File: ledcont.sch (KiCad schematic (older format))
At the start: 22 parts, among them J1 Screw_Terminal_01x02, J2 Screw_Terminal_01x02, U1 PAM2804, U2 TSM102A

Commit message: Switched PAM2804 to a standard TSOT-23-5 footprint.
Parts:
- U1: footprint ledcont:TSOT25 -> Package_TO_SOT_SMD:TSOT-23-5_HandSoldering
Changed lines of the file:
@@
 F 0 "U1" H 6550 2665 50  0000 C CNN
 F 1 "PAM2804" H 6550 2574 50  0000 C CNN
-F 2 "ledcont:TSOT25" H 6550 2250 50  0001 C CNN
+F 2 "Package_TO_SOT_SMD:TSOT-23-5_HandSoldering" H 6550 2250 50  0001 C CNN
 F 3 "" H 6550 2250 50  0001 C CNN
 F 4 "PAM2804AAB010" H 0   0   50  0001 C CNN "Part"

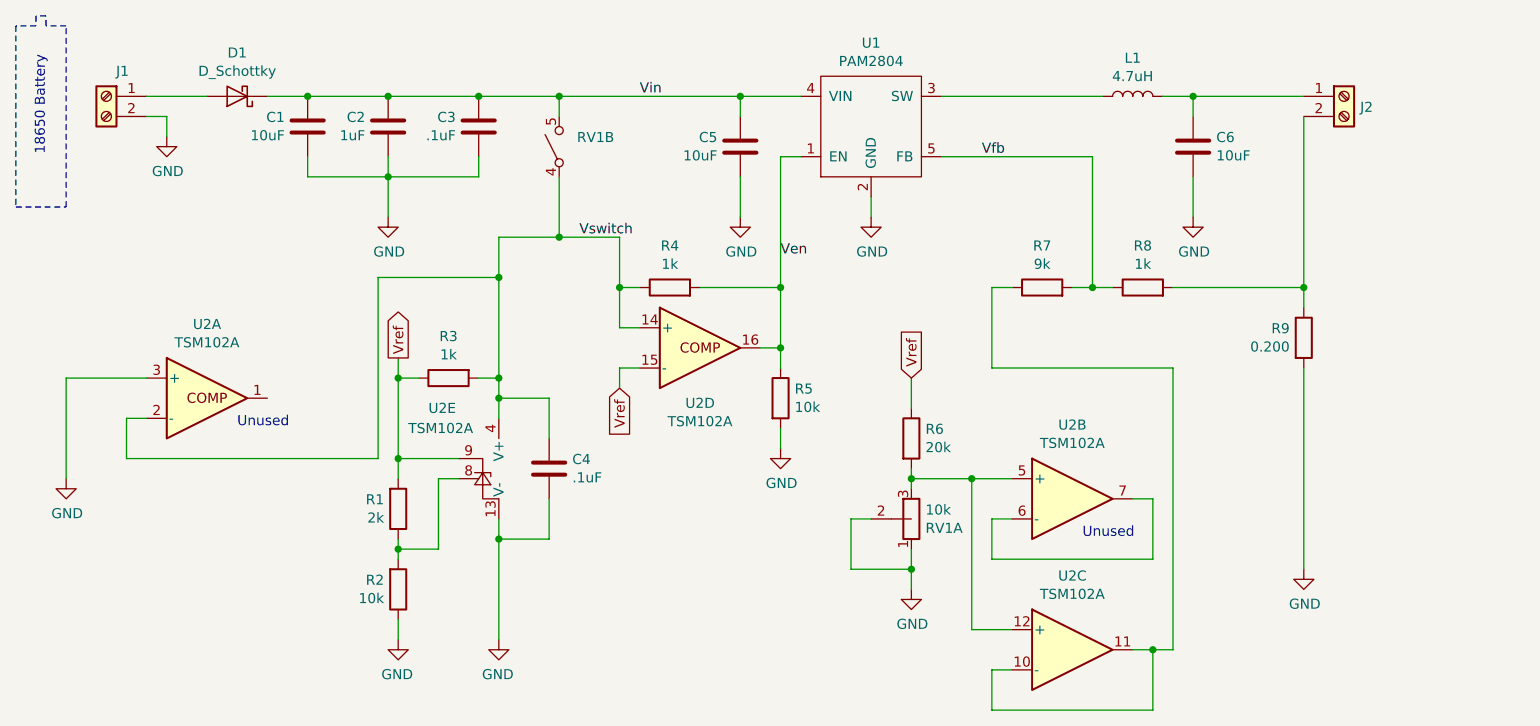
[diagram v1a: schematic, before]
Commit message: Start transitioning to lower-voltage parts.
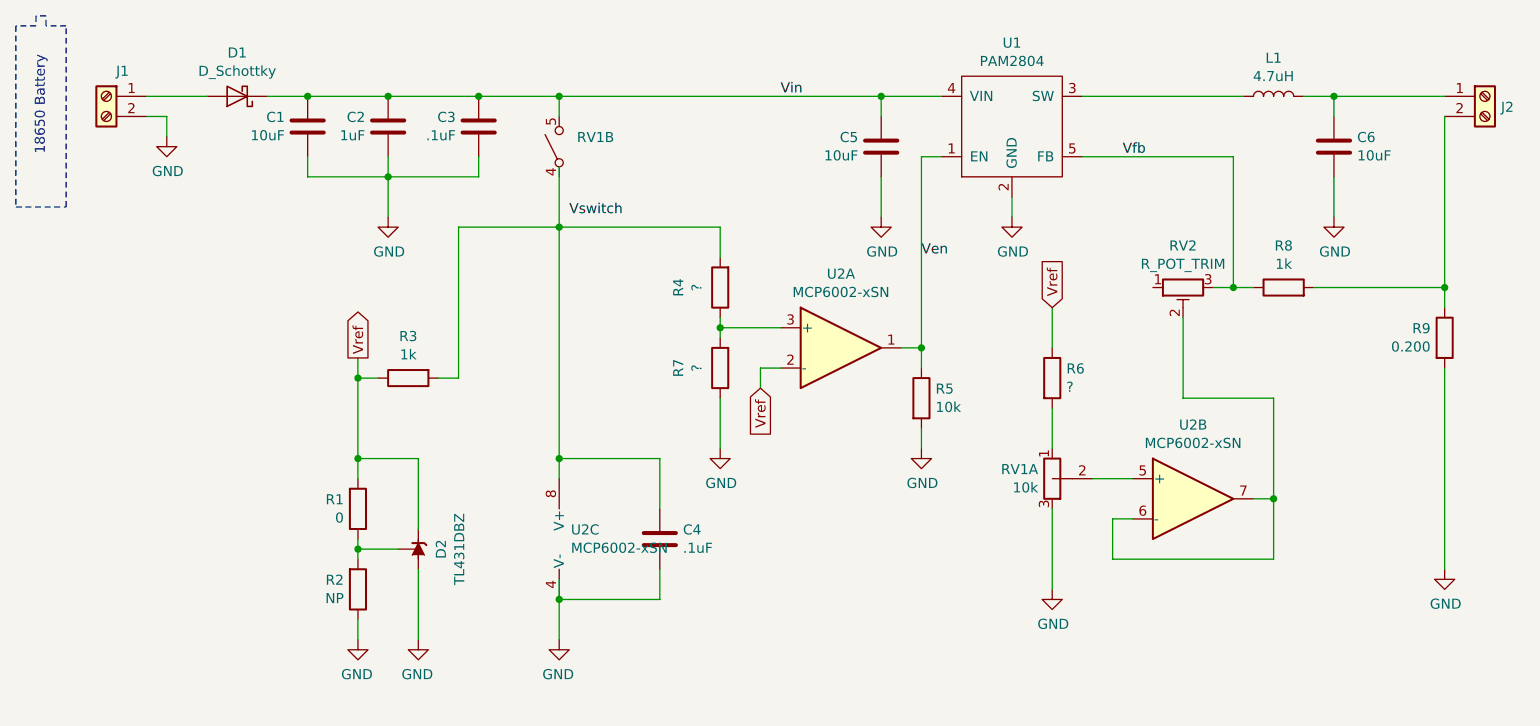
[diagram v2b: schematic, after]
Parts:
- removed U2: TSM102A, Package_SO:SOIC-16_3.9x9.9mm_P1.27mm, symbol Power_Management:TSM102A
- added D2: TL431DBZ, Package_TO_SOT_SMD:SOT-23, symbol Reference_Voltage:TL431DBZ
- added RV2: R_POT_TRIM, symbol Device:R_POT_TRIM
- added U2: MCP6002-xSN, Package_SO:SOIC-8_3.9x4.9mm_P1.27mm, symbol Amplifier_Operational:MCP6002-xSN
- R1: value 2k -> 0
- R2: value 10k -> NP
- R4: value 1k -> ?
- R6: value 20k -> ?
- R7: value 9k -> ?
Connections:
- net GND: now also R7.1, RV1.3, D2.3 (A), U2.4 (V-); no longer RV1.1, RV1.2 (B)
- net Ven: now also U2.1; no longer R4.2
- net Vfb: now also RV2.3; no longer R7.2
- net Vref: now also D2.1 (K), U2.2 (-)
- net Vswitch: no longer C4.1, R3.2, R4.1, RV1.4
- net at R6.2: now also RV1.1; no longer RV1.3
- net at R1.1, R2.2: now also D2.2 (REF)
- new net: RV1.2 (B), U2.5 (+)
- new net: C4.1, R3.2, R4.2, U2.8 (V+)
- new net: R4.1, R7.2, U2.3 (+)
- new net: RV2.2, U2.6 (-), U2.7
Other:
- note removed: "Unused"
- moved on the sheet: C4, C5, C6, J2, L1, R1, R2, R3, R5, R6, R8, R9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

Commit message: More board updates.
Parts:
- added R10: 10k, Resistor_SMD:R_0603_1608Metric_Pad1.05x0.95mm_HandSolder, symbol Device:R
- added R11, R12: 0, Resistor_SMD:R_0603_1608Metric_Pad1.05x0.95mm_HandSolder, symbol Device:R
- D2: value TL431DBZ -> TLV431
- R1, R2, R3, R5: footprint Resistor_SMD:R_1206_3216Metric_Pad1.42x1.75mm_HandSolder -> Resistor_SMD:R_0603_1608Metric_Pad1.05x0.95mm_HandSolder
- R4: value ? -> 10k; footprint Resistor_SMD:R_1206_3216Metric_Pad1.42x1.75mm_HandSolder -> Resistor_SMD:R_0603_1608Metric_Pad1.05x0.95mm_HandSolder
- R6: value ? -> 0; footprint Resistor_SMD:R_1206_3216Metric_Pad1.42x1.75mm_HandSolder -> Resistor_SMD:R_0603_1608Metric_Pad1.05x0.95mm_HandSolder
- R7: value ? -> 7k; footprint Resistor_SMD:R_1206_3216Metric_Pad1.42x1.75mm_HandSolder -> Resistor_SMD:R_0603_1608Metric_Pad1.05x0.95mm_HandSolder
- RV2: value R_POT_TRIM -> 5k; footprint (none) -> ledcont:TC33X
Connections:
- net Ven: now also R12.2; no longer U1.1 (EN)
- net Vfb: now also R10.2; no longer RV2.3
- net Vswitch: now also C4.1, R3.2, R4.2, RV1.4, U2.8 (V+)
- net at U2.6 (-), U2.7: now also R11.2; no longer RV2.2
- net at RV2.1: now also RV2.2, R11.1
- new net: R12.1, U1.1 (EN)
- new net: R10.1, RV2.3
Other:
- moved on the sheet: R6, RV1A, RV2
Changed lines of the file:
@@
 L ledcont:R_POT_SPST RV1
 U 1 1 5C458CC6
-P 7450 4000
-F 0 "RV1" H 7380 3954 50  0000 R CNN
-F 1 "10k" H 7380 4045 50  0000 R CNN
-F 2 "ledcont:P091_S" H 7450 4000 50  0001 C CNN
-F 3 "~" H 7450 4000 50  0001 C CNN
-F 4 "P091S-FC20BR10K" H 700 -200 50  0001 C CNN "Part"
-	1    7450 4000
+P 7250 4000
+F 0 "RV1" H 7180 3954 50  0000 R CNN
+F 1 "10k" H 7180 4045 50  0000 R CNN
+F 2 "ledcont:P091_S" H 7250 4000 50  0001 C CNN
+F 3 "~" H 7250 4000 50  0001 C CNN
+F 4 "P091S-FC20BR10K" H 500 -200 50  0001 C CNN "Part"
+	1    7250 4000
 	1    0    0    1
 $EndComp
@@
 F 0 "R3" V 4043 3500 50  0000 C CNN
 F 1 "1k" V 4134 3500 50  0000 C CNN
-F 2 "Resistor_SMD:R_1206_3216Metric_Pad1.42x1.75mm_HandSolder" V 4180 3500 50  0001 C CNN
+F 2 "Resistor_SMD:R_0603_1608Metric_Pad1.05x0.95mm_HandSolder" V 4180 3500 50  0001 C CNN
 F 3 "~" H 4250 3500 50  0001 C CNN
 F 4 "1%" H -200 0   50  0001 C CNN "Tolerance"
@@
 F 0 "R1" H 3930 4104 50  0000 R CNN
 F 1 "0" H 3930 4195 50  0000 R CNN
-F 2 "Resistor_SMD:R_1206_3216Metric_Pad1.42x1.75mm_HandSolder" V 3930 4150 50  0001 C CNN
+F 2 "Resistor_SMD:R_0603_1608Metric_Pad1.05x0.95mm_HandSolder" V 3930 4150 50  0001 C CNN
 F 3 "~" H 4000 4150 50  0001 C CNN
 F 4 "1%" H 4000 4150 50  0001 C CNN "Tolerance"
@@
 F 0 "R2" H 3930 4504 50  0000 R CNN
 F 1 "NP" H 3930 4595 50  0000 R CNN
-F 2 "Resistor_SMD:R_1206_3216Metric_Pad1.42x1.75mm_HandSolder" V 3930 4550 50  0001 C CNN
+F 2 "Resistor_SMD:R_0603_1608Metric_Pad1.05x0.95mm_HandSolder" V 3930 4550 50  0001 C CNN
 F 3 "~" H 4000 4550 50  0001 C CNN
 F 4 "1%" H -200 0   50  0001 C CNN "Tolerance"
@@
 L Device:R R6
 U 1 1 5C482FDC
-P 7450 3500
-F 0 "R6" H 7520 3546 50  0000 L CNN
-F 1 "?" H 7520 3455 50  0000 L CNN
-F 2 "Resistor_SMD:R_1206_3216Metric_Pad1.42x1.75mm_HandSolder" V 7380 3500 50  0001 C CNN
-F 3 "~" H 7450 3500 50  0001 C CNN
-F 4 "RC1206FR-0720KL" H 700 -300 50  0001 C CNN "Part"
-	1    7450 3500
+P 7250 3500
+F 0 "R6" H 7320 3546 50  0000 L CNN
+F 1 "0" H 7320 3455 50  0000 L CNN
+F 2 "Resistor_SMD:R_0603_1608Metric_Pad1.05x0.95mm_HandSolder" V 7180 3500 50  0001 C CNN
+F 3 "~" H 7250 3500 50  0001 C CNN
+F 4 "RC1206FR-0720KL" H 500 -300 50  0001 C CNN "Part"
+	1    7250 3500
 	1    0    0    -1
 $EndComp
@@
 L power:GND #PWR011
 U 1 1 5C4859F5
-P 7450 4550
-F 0 "#PWR011" H 7450 4300 50  0001 C CNN
-F 1 "GND" H 7455 4377 50  0000 C CNN
-F 2 "" H 7450 4550 50  0001 C CNN
-F 3 "" H 7450 4550 50  0001 C CNN
-	1    7450 4550
-	1    0    0    -1
-$EndComp
-Text GLabel 7450 3150 1    50   Input ~ 0
+P 7250 4550
+F 0 "#PWR011" H 7250 4300 50  0001 C CNN
+F 1 "GND" H 7255 4377 50  0000 C CNN
+F 2 "" H 7250 4550 50  0001 C CNN
+F 3 "" H 7250 4550 50  0001 C CNN
+	1    7250 4550
+	1    0    0    -1
+$EndComp
+Text GLabel 7250 3150 1    50   Input ~ 0
 Vref
 Wire Wire Line
-	7450 3150 7450 3350
+	7250 3150 7250 3350
 Wire Notes Line
 	2300 1750 2300 2650
@@
 F 0 "R5" H 6870 3646 50  0000 L CNN
 F 1 "10k" H 6870 3555 50  0000 L CNN
-F 2 "Resistor_SMD:R_1206_3216Metric_Pad1.42x1.75mm_HandSolder" V 6730 3600 50  0001 C CNN
+F 2 "Resistor_SMD:R_0603_1608Metric_Pad1.05x0.95mm_HandSolder" V 6730 3600 50  0001 C CNN
 F 3 "~" H 6800 3600 50  0001 C CNN
 F 4 "1%" H 700 0   50  0001 C CNN "Tolerance"
@@
 Wire Wire Line
 	6800 3750 6800 3850
-Wire Wire Line
-	8350 3050 8250 3050
-Connection ~ 8350 3050
 Text GLabel 6000 3550 3    50   Input ~ 0
 Vref
@@
 	1    0    0    -1
 $EndComp
-Text Label 5050 2700 0    50   ~ 0
-Vswitch
 Text Label 6100 2100 0    50   ~ 0
 Vin
@@
 P 4300 4350
 F 0 "D2" H 4300 4236 50  0000 C CNN
-F 1 "TL431DBZ" H 4300 4145 50  0000 C CNN
+F 1 "TLV431" H 4300 4145 50  0000 C CNN
 F 2 "Package_TO_SOT_SMD:SOT-23" H 4300 4200 50  0001 C CIN
 F 3 "http://www.ti.com/lit/ds/symlink/tl431.pdf" H 4300 4350 50  0001 C CIN
@@
 	5000 2750 5000 3900
 Wire Wire Line
-	6800 2400 6800 3350
+	6800 2400 6800 2600
 Wire Wire Line
 	5000 2100 6600 2100
@@
 P 5800 3050
 F 0 "R4" V 6007 3050 50  0000 C CNN
-F 1 "?" V 5916 3050 50  0000 C CNN
-F 2 "Resistor_SMD:R_1206_3216Metric_Pad1.42x1.75mm_HandSolder" V 5730 3050 50  0001 C CNN
+F 1 "10k" V 5916 3050 50  0000 C CNN
+F 2 "Resistor_SMD:R_0603_1608Metric_Pad1.05x0.95mm_HandSolder" V 5730 3050 50  0001 C CNN
 F 3 "~" H 5800 3050 50  0001 C CNN
 F 4 "1%" H -2100 0   50  0001 C CNN "Tolerance"
@@
 P 5800 3450
 F 0 "R7" V 6007 3450 50  0000 C CNN
-F 1 "?" V 5916 3450 50  0000 C CNN
-F 2 "Resistor_SMD:R_1206_3216Metric_Pad1.42x1.75mm_HandSolder" V 5730 3450 50  0001 C CNN
+F 1 "7k" V 5916 3450 50  0000 C CNN
+F 2 "Resistor_SMD:R_0603_1608Metric_Pad1.05x0.95mm_HandSolder" V 5730 3450 50  0001 C CNN
 F 3 "~" H 5800 3450 50  0001 C CNN
 F 4 "RC1206FR-079K09L" H -1600 400 50  0001 C CNN "Part"
@@
 	7750 4200 7850 4200
 Wire Wire Line
-	7450 4150 7450 4550
-Wire Wire Line
-	7450 3650 7450 3850
-Wire Wire Line
-	7650 4000 7850 4000
+	7250 4150 7250 4550
+Wire Wire Line
+	7250 3650 7250 3850
+Wire Wire Line
+	7450 4000 7850 4000
 $Comp
 L Device:R_POT_TRIM RV2
 U 1 1 5C667481
+P 7700 3050
+F 0 "RV2" V 7493 3050 50  0000 C CNN
+F 1 "5k" V 7584 3050 50  0000 C CNN
+F 2 "ledcont:TC33X" H 7700 3050 50  0001 C CNN
+F 3 "~" H 7700 3050 50  0001 C CNN
+	1    7700 3050
+	0    -1   1    0
+$EndComp
+Wire Wire Line
+	7700 3200 7700 3300
+Wire Wire Line
+	7700 3600 8550 3600
+Wire Wire Line
+	8550 3600 8550 3700
+Connection ~ 8550 4100
+Wire Wire Line
+	5000 2500 5000 2750
+$Comp
+L Device:R R10
+U 1 1 5C5DEEB7
 P 8100 3050
-F 0 "RV2" V 7893 3050 50  0000 C CNN
-F 1 "R_POT_TRIM" V 7984 3050 50  0000 C CNN
-F 2 "" H 8100 3050 50  0001 C CNN
+F 0 "R10" V 8307 3050 50  0000 C CNN
+F 1 "10k" V 8216 3050 50  0000 C CNN
+F 2 "Resistor_SMD:R_0603_1608Metric_Pad1.05x0.95mm_HandSolder" V 8030 3050 50  0001 C CNN
 F 3 "~" H 8100 3050 50  0001 C CNN
+F 4 "1%" H 200 0   50  0001 C CNN "Tolerance"
+F 5 "RC1206FR-071KL" H 200 0   50  0001 C CNN "Part"
 	1    8100 3050
-	0    -1   1    0
-$EndComp
-Wire Wire Line
-	8100 3200 8100 3600
-Wire Wire Line
-	8100 3600 8550 3600
-Wire Wire Line
-	8550 3600 8550 4100
-Connection ~ 8550 4100
-Wire Wire Line
-	5000 2450 5000 2750
+	0    -1   -1   0
+$EndComp
+Wire Wire Line
+	8250 3050 8350 3050
+Connection ~ 8350 3050
+Wire Wire Line
+	7850 3050 7950 3050
+Wire Wire Line
+	7550 3050 7450 3050
+Wire Wire Line
+	7450 3050 7450 3300
+Wire Wire Line
+	7450 3300 7700 3300
+Connection ~ 7700 3300
+Wire Wire Line
+	7700 3300 7700 3600
+Text Label 5250 2750 0    50   ~ 0
+Vswitch
+$Comp
+L Device:R R11
+U 1 1 5C5FFECD
+P 8550 3850
+F 0 "R11" H 8620 3896 50  0000 L CNN
+F 1 "0" H 8620 3805 50  0000 L CNN
+F 2 "Resistor_SMD:R_0603_1608Metric_Pad1.05x0.95mm_HandSolder" V 8480 3850 50  0001 C CNN
+F 3 "~" H 8550 3850 50  0001 C CNN
+F 4 "RC1206FR-0720KL" H 1800 50  50  0001 C CNN "Part"
+	1    8550 3850
+	1    0    0    -1
+$EndComp
+Wire Wire Line
+	8550 4000 8550 4100
+$Comp
+L Device:R R12
+U 1 1 5C604BE5
+P 6800 2750
+F 0 "R12" H 6870 2796 50  0000 L CNN
+F 1 "0" H 6870 2705 50  0000 L CNN
+F 2 "Resistor_SMD:R_0603_1608Metric_Pad1.05x0.95mm_HandSolder" V 6730 2750 50  0001 C CNN
+F 3 "~" H 6800 2750 50  0001 C CNN
+F 4 "RC1206FR-0720KL" H 50  -1050 50  0001 C CNN "Part"
+	1    6800 2750
+	1    0    0    -1
+$EndComp
+Wire Wire Line
+	6800 2900 6800 3350
 $EndSCHEMATC

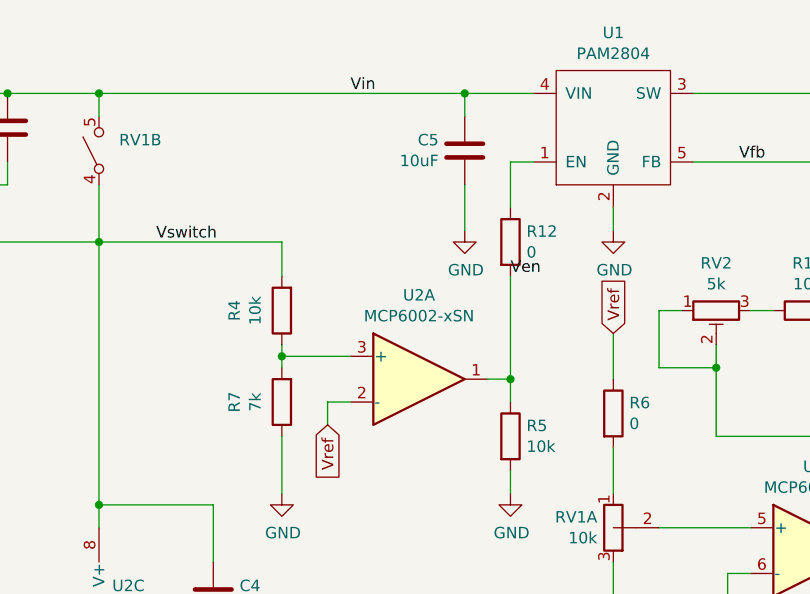
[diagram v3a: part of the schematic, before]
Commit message: More work to get things ordered.  Updated the BoM.
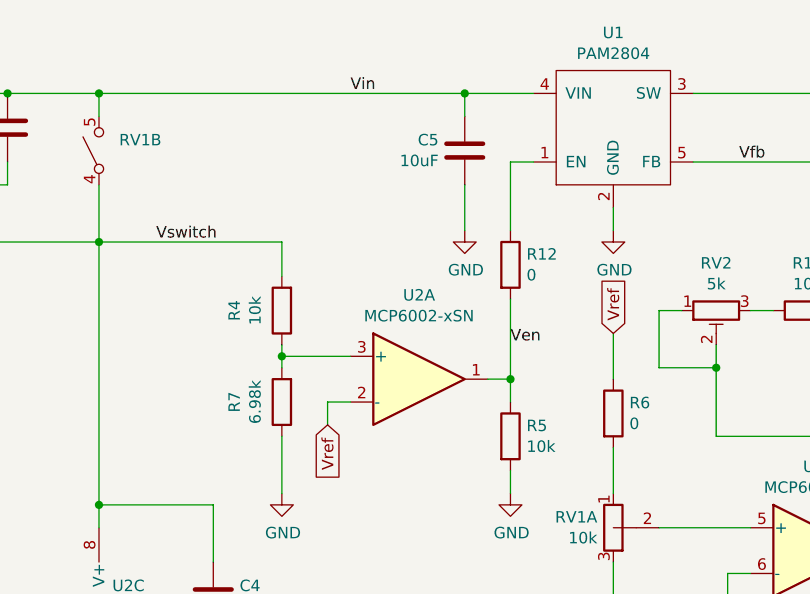
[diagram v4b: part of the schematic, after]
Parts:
- R1: Part RC1206FR-072KL -> RC0603FR-070RL
- R10, R4: Part RC1206FR-071KL -> RC0603FR-0710KL
- R11, R12, R6: Part RC1206FR-0720KL -> RC0603FR-070RL
- R2: Part RC1206FR-0710KL -> (none)
- R3: Part RC1206FR-071KL -> RC0603FR-071KL
- R5: Part RC1206FR-0710KL -> RC0603FR-0710KL
- R7: value 7k -> 6.98k; Part RC1206FR-079K09L -> RC0603FR-076K98L
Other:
- moved on the sheet: R12
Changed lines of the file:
@@
 F 3 "~" H 4250 3500 50  0001 C CNN
 F 4 "1%" H -200 0   50  0001 C CNN "Tolerance"
-F 5 "RC1206FR-071KL" V 4250 3500 50  0001 C CNN "Part"
+F 5 "RC0603FR-071KL" V 4250 3500 50  0001 C CNN "Part"
 	1    4250 3500
 	0    -1   1    0
@@
 F 3 "~" H 4000 4150 50  0001 C CNN
 F 4 "1%" H 4000 4150 50  0001 C CNN "Tolerance"
-F 5 "RC1206FR-072KL" H -200 0   50  0001 C CNN "Part"
+F 5 "RC0603FR-070RL" H -200 0   50  0001 C CNN "Part"
 	1    4000 4150
 	1    0    0    1
@@
 F 3 "~" H 4000 4550 50  0001 C CNN
 F 4 "1%" H -200 0   50  0001 C CNN "Tolerance"
-F 5 "RC1206FR-0710KL" H -200 0   50  0001 C CNN "Part"
+F 5 "" H -200 0   50  0001 C CNN "Part"
 	1    4000 4550
 	1    0    0    1
@@
 F 2 "Resistor_SMD:R_0603_1608Metric_Pad1.05x0.95mm_HandSolder" V 7180 3500 50  0001 C CNN
 F 3 "~" H 7250 3500 50  0001 C CNN
-F 4 "RC1206FR-0720KL" H 500 -300 50  0001 C CNN "Part"
+F 4 "RC0603FR-070RL" H 500 -300 50  0001 C CNN "Part"
 	1    7250 3500
 	1    0    0    -1
@@
 F 3 "~" H 6800 3600 50  0001 C CNN
 F 4 "1%" H 700 0   50  0001 C CNN "Tolerance"
-F 5 "RC1206FR-0710KL" H 700 0   50  0001 C CNN "Part"
+F 5 "RC0603FR-0710KL" H 700 0   50  0001 C CNN "Part"
 	1    6800 3600
 	1    0    0    -1
@@
 Text Label 7800 2400 0    50   ~ 0
 Vfb
-Text Label 6800 2900 0    50   ~ 0
-Ven
 $Comp
 L Amplifier_Operational:MCP6002-xSN U2
@@
 	5000 2750 5000 3900
 Wire Wire Line
-	6800 2400 6800 2600
+	6800 2400 6800 2700
 Wire Wire Line
 	5000 2100 6600 2100
@@
 F 3 "~" H 5800 3050 50  0001 C CNN
 F 4 "1%" H -2100 0   50  0001 C CNN "Tolerance"
-F 5 "RC1206FR-071KL" H -2100 0   50  0001 C CNN "Part"
+F 5 "RC0603FR-0710KL" H -2100 0   50  0001 C CNN "Part"
 	1    5800 3050
 	-1   0    0    1
@@
 P 5800 3450
 F 0 "R7" V 6007 3450 50  0000 C CNN
-F 1 "7k" V 5916 3450 50  0000 C CNN
+F 1 "6.98k" V 5916 3450 50  0000 C CNN
 F 2 "Resistor_SMD:R_0603_1608Metric_Pad1.05x0.95mm_HandSolder" V 5730 3450 50  0001 C CNN
 F 3 "~" H 5800 3450 50  0001 C CNN
-F 4 "RC1206FR-079K09L" H -1600 400 50  0001 C CNN "Part"
+F 4 "RC0603FR-076K98L" H -1600 400 50  0001 C CNN "Part"
 F 5 "1%" H -1600 400 50  0001 C CNN "Tolerance"
 	1    5800 3450
@@
 F 3 "~" H 8100 3050 50  0001 C CNN
 F 4 "1%" H 200 0   50  0001 C CNN "Tolerance"
-F 5 "RC1206FR-071KL" H 200 0   50  0001 C CNN "Part"
+F 5 "RC0603FR-0710KL" H 200 0   50  0001 C CNN "Part"
 	1    8100 3050
 	0    -1   -1   0
@@
 F 2 "Resistor_SMD:R_0603_1608Metric_Pad1.05x0.95mm_HandSolder" V 8480 3850 50  0001 C CNN
 F 3 "~" H 8550 3850 50  0001 C CNN
-F 4 "RC1206FR-0720KL" H 1800 50  50  0001 C CNN "Part"
+F 4 "RC0603FR-070RL" H 1800 50  50  0001 C CNN "Part"
 	1    8550 3850
 	1    0    0    -1
@@
 L Device:R R12
 U 1 1 5C604BE5
-P 6800 2750
-F 0 "R12" H 6870 2796 50  0000 L CNN
-F 1 "0" H 6870 2705 50  0000 L CNN
-F 2 "Resistor_SMD:R_0603_1608Metric_Pad1.05x0.95mm_HandSolder" V 6730 2750 50  0001 C CNN
-F 3 "~" H 6800 2750 50  0001 C CNN
-F 4 "RC1206FR-0720KL" H 50  -1050 50  0001 C CNN "Part"
-	1    6800 2750
-	1    0    0    -1
-$EndComp
-Wire Wire Line
-	6800 2900 6800 3350
+P 6800 2850
+F 0 "R12" H 6870 2896 50  0000 L CNN
+F 1 "0" H 6870 2805 50  0000 L CNN
+F 2 "Resistor_SMD:R_0603_1608Metric_Pad1.05x0.95mm_HandSolder" V 6730 2850 50  0001 C CNN
+F 3 "~" H 6800 2850 50  0001 C CNN
+F 4 "RC0603FR-070RL" H 50  -950 50  0001 C CNN "Part"
+	1    6800 2850
+	1    0    0    -1
+$EndComp
+Wire Wire Line
+	6800 3000 6800 3350
+Text Label 6800 3200 0    50   ~ 0
+Ven
 $EndSCHEMATC

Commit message: Updated the schematic.  Fixed missing PNs.
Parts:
- D2: Part (none) -> TLV431AFTA
- RV2: Part (none) -> TC33X-2-502E
- U2: Part (none) -> MCP6002T-I/SN
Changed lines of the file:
@@
 F 2 "Package_SO:SOIC-8_3.9x4.9mm_P1.27mm" H 6400 3350 50  0001 C CNN
 F 3 "http://ww1.microchip.com/downloads/en/DeviceDoc/21733j.pdf" H 6400 3350 50  0001 C CNN
+F 4 "MCP6002T-I/SN" H 0   0   50  0001 C CNN "Part"
 	1    6400 3350
 	1    0    0    -1
@@
 F 2 "Package_SO:SOIC-8_3.9x4.9mm_P1.27mm" H 8150 4100 50  0001 C CNN
 F 3 "http://ww1.microchip.com/downloads/en/DeviceDoc/21733j.pdf" H 8150 4100 50  0001 C CNN
+F 4 "MCP6002T-I/SN" H 0   0   50  0001 C CNN "Part"
 	2    8150 4100
 	1    0    0    -1
@@
 F 2 "Package_SO:SOIC-8_3.9x4.9mm_P1.27mm" H 5100 4300 50  0001 C CNN
 F 3 "http://ww1.microchip.com/downloads/en/DeviceDoc/21733j.pdf" H 5100 4300 50  0001 C CNN
+F 4 "MCP6002T-I/SN" H 0   0   50  0001 C CNN "Part"
 	3    5100 4300
 	1    0    0    -1
@@
 F 2 "Package_TO_SOT_SMD:SOT-23" H 4300 4200 50  0001 C CIN
 F 3 "http://www.ti.com/lit/ds/symlink/tl431.pdf" H 4300 4350 50  0001 C CIN
+F 4 "TLV431AFTA" H 4300 4350 50  0001 C CNN "Part"
 	1    4300 4350
 	0    -1   -1   0
@@
 F 2 "ledcont:TC33X" H 7700 3050 50  0001 C CNN
 F 3 "~" H 7700 3050 50  0001 C CNN
+F 4 "TC33X-2-502E" V 7700 3050 50  0001 C CNN "Part"
 	1    7700 3050
 	0    -1   1    0
